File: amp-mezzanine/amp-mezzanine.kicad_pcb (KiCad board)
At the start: 2 copper layers, 26 parts, among them J1 LOGIC_IN, J2 I2C

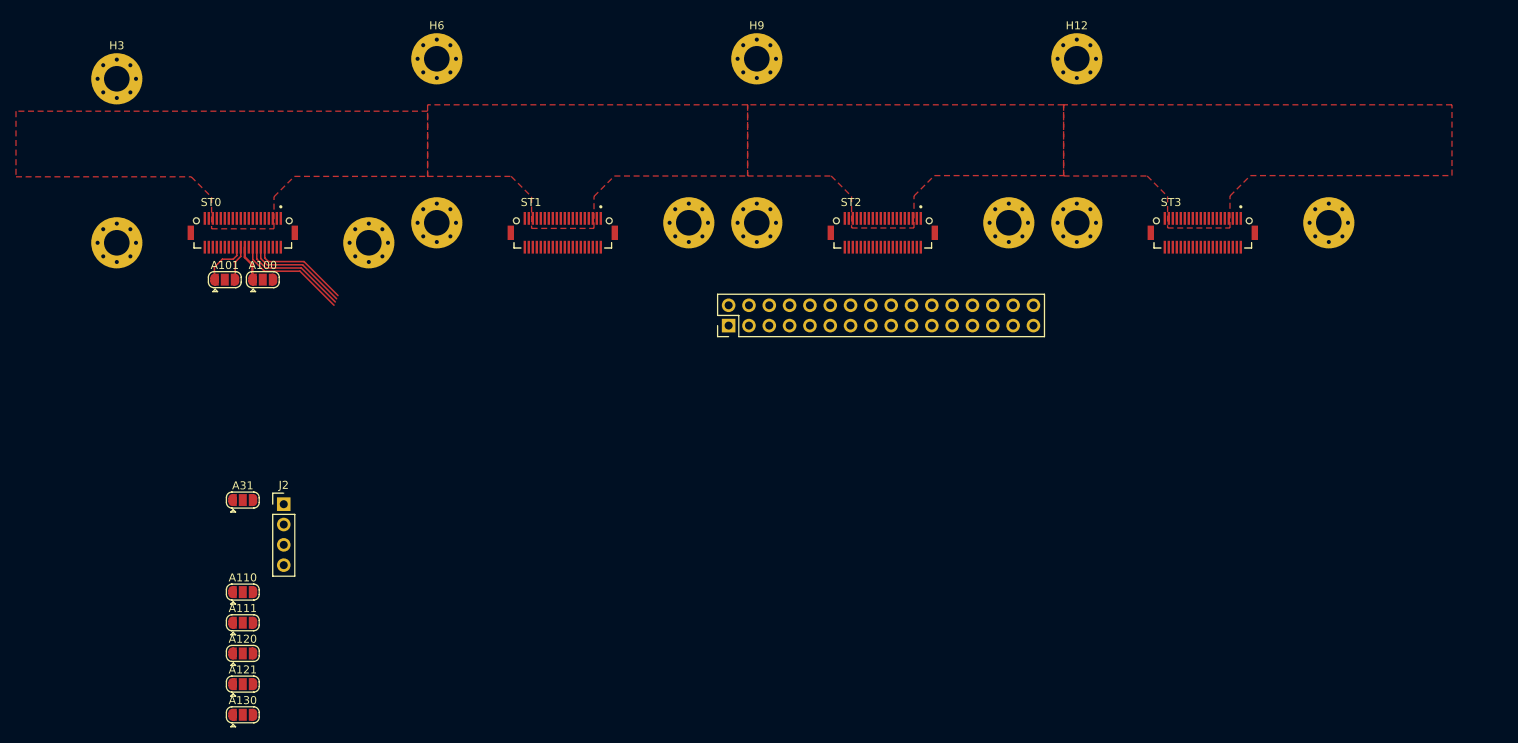
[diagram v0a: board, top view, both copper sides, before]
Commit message: Finished mezzanine layout
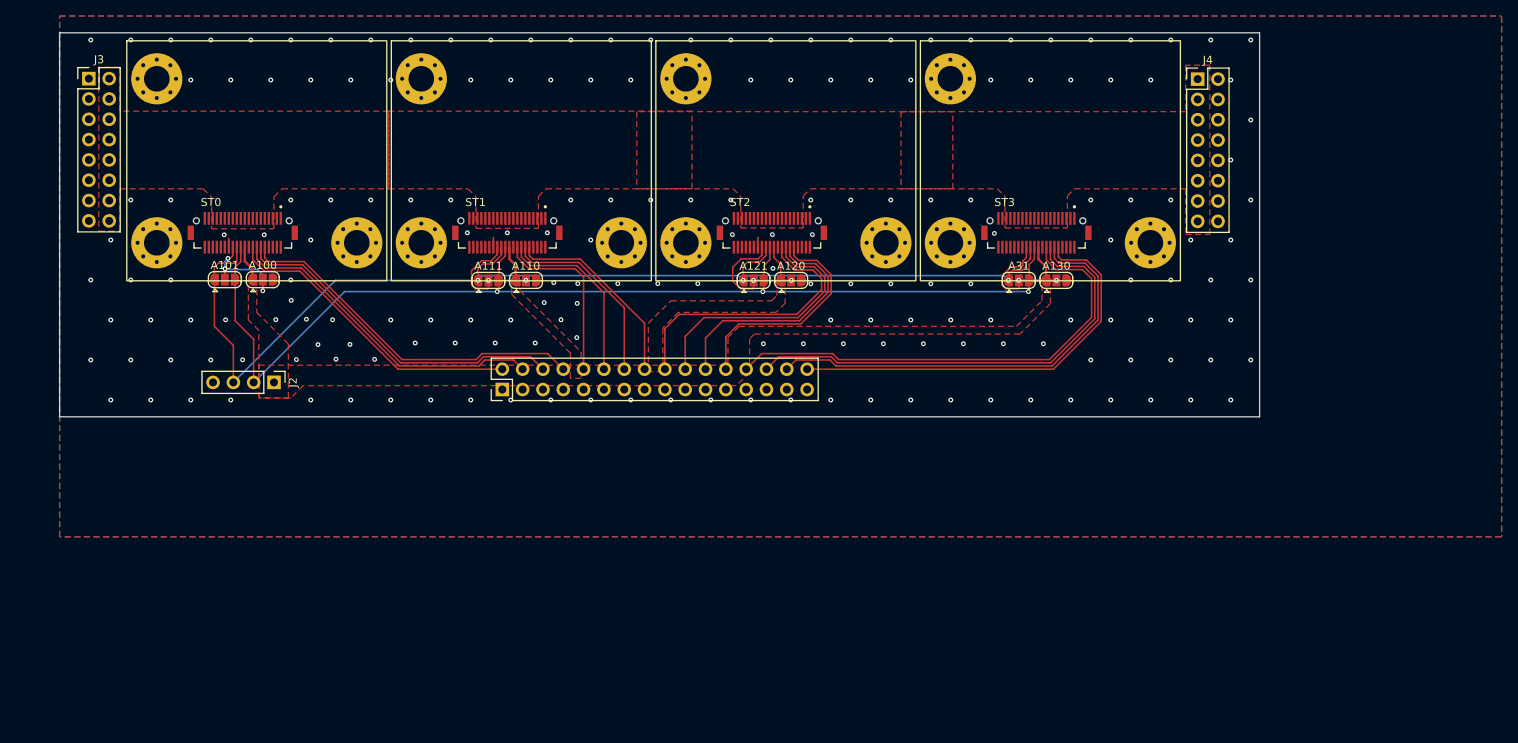
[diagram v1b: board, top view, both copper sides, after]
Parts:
- removed H1, H10, H11, H12, H2, H3, H4, H5, H6, H7, H8, H9: MountingHole_Pad, MountingHole:MountingHole_3.2mm_M3_Pad_Via
- added J3: PWR_A, Connector_PinHeader_2.54mm:PinHeader_2x08_P2.54mm_Vertical, F.Cu at (73.7, 57.7)
- added J4: PWR_B, Connector_PinHeader_2.54mm:PinHeader_2x08_P2.54mm_Vertical, F.Cu at (212.3, 57.8)
- A100: value SolderJumper_3_Open -> GND
- A101, A111, A120, A130: value SolderJumper_3_Open -> NC
- A110: value SolderJumper_3_Open -> 3V3
- A121: value SolderJumper_3_Open -> SDA
- A31: value SolderJumper_3_Open -> SCL
- ST0, ST1, ST2, ST3: footprint project_footprints:AMPHENOL_10132797-045100LF -> project_footprints:PICCDAC-AMPHENOL-10132797-045100LF
- moved A130 115.3 mm to (194.6, 83.0)
- moved A31 100.8 mm to (189.9, 83.0)
- moved A120 82.9 mm to (161.4, 83.0)
- moved A121 81.4 mm to (156.8, 83.0)
- moved A111 52.7 mm to (123.6, 83.0)
- moved A110 52.6 mm to (128.3, 83.0)
- moved J1 29.4 mm to (125.3, 96.6)
- moved ST3 20.8 mm to (192.1, 77.0)
- moved J2 15.3 mm to (96.8, 95.7), turned to -90 degrees
- moved ST2 13.9 mm to (159.0, 77.0)
- moved ST1 6.93 mm to (126.0, 77.0)
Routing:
- net /SCL: track 5.25 -> 140.9 mm, vias 0 -> 3
- net /SDA: track 3.59 -> 136.7 mm, vias 0 -> 3
- net /CTRL_D3: track 0.00 -> 59.5 mm
- net /CTRL_C3: track 0.00 -> 57.4 mm
- net /CTRL_B3: track 0.00 -> 55.3 mm
- net /CTRL_A3: track 0.00 -> 52.5 mm
- net /CTRL_D2: track 0.00 -> 35.4 mm
- net /CTRL_C2: track 0.00 -> 32.7 mm
- net /CTRL_A0: track 12.4 -> 45.0 mm
- net /CTRL_B2: track 0.00 -> 30.5 mm
- net /CTRL_B0: track 13.0 -> 43.0 mm
- net /CTRL_A2: track 0.00 -> 28.5 mm
- net /CTRL_C0: track 13.5 -> 41.0 mm
- net /CTRL_A1: track 0.00 -> 24.7 mm
- net /CTRL_D0: track 14.1 -> 38.4 mm
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- added copper zone on F.Cu, net +3V3
- added copper zone on B.Cu, net GND
- added copper zone on F.Cu, net GND
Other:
- board outline added: 150 x 48 mm
